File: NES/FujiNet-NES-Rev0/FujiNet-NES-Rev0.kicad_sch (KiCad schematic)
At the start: 0 parts

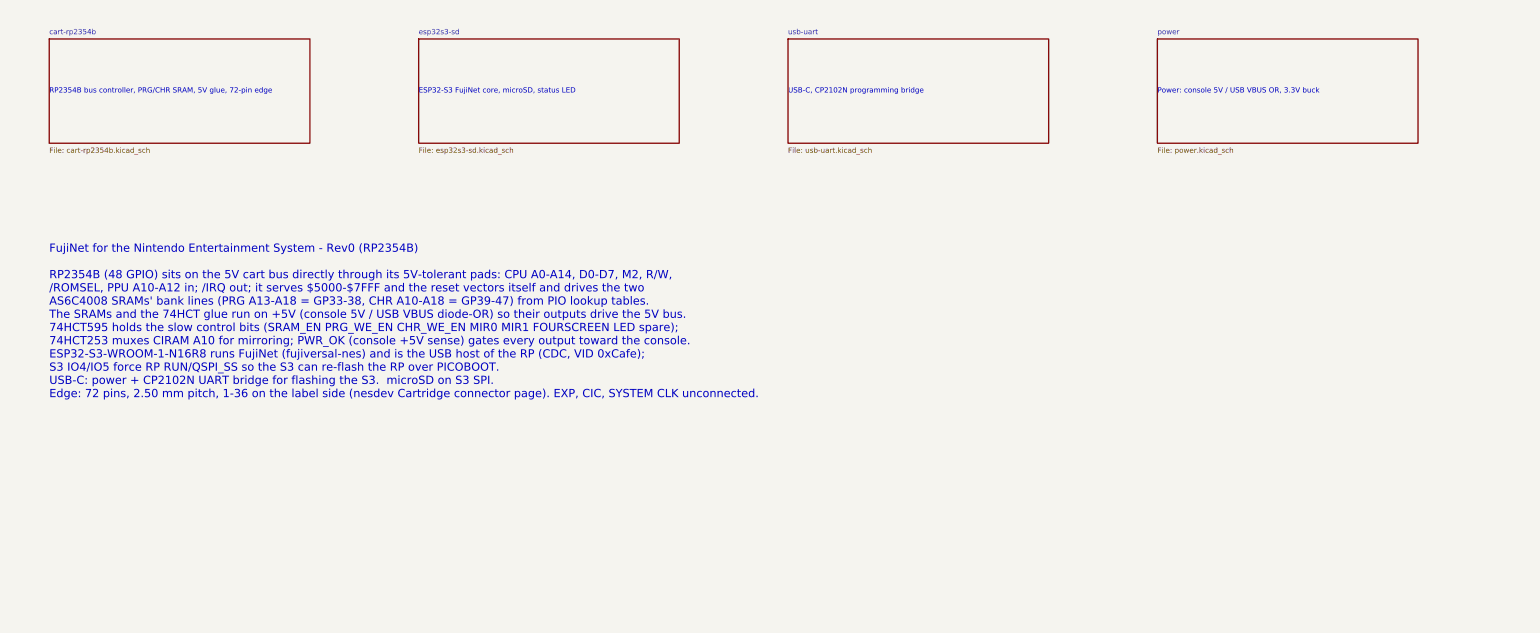
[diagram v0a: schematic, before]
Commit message: Nes rev0 (#48)
* NES: add the FujiNet-NES-Rev0 schematic

RP2354B on the 5 V cart bus with two AS6C4008-55 SRAMs (PRG, CHR) whose
bank lines come from the RP's PIO, 74HCT595/253/14/00/32 glue, and the
Astrocade Rev0 ESP32-S3, USB-UART and power sheets carried over.
Generated from tools/design.py the same way as Astrocade/rev0; ERC
reports no violations and tools/check_nets.py checks every GPIO, SRAM
line and decode equation against fujinet-firmware's nes_cart.h and
fujiversal-nes.h.

Schematic only: no layout, no board built, nothing run on a console.
The edge pinout follows the nesdev Cartridge connector page (pin 37 is
SYSTEM CLK, 2.50 mm pitch).

Co-Authored-By: Claude Fable 5.1 <noreply@anthropic.com>

* NES Rev0: audit the schematic with kicad-happy and redo it

Datasheet-backed review of the first Rev0 schematic (kicad-happy analyzer,
ngspice, 28 deep-review findings all evidence-gated, 453 netlist checks
against fujinet-firmware nes-bringup) and the fixes it called for:

- edge footprint was mirrored (pin 1 west); nesdev and two measured
  NES-EWROM-01 references put pin 1 east on the label side. Fingers are now
  2.0 x 12 mm (ends 3.0 at +/-44.25), 2.50 pitch, copper 1.0-13.0 mm in,
  Nintendo's front/back mask depths
- RP2350 pads are 5 V-tolerant only while IOVDD is powered: the IOVDD group
  moves to an AP2112K (20 us) rail +3V3_RP; VREG_VIN stays on the buck
- 74HCT595 /OE = NAND(PWR_OK, POR) with 100k pull-downs on every bit, so
  the register cannot enable the SRAMs before the RP loads it or while
  the console is off
- PRG /WE = NAND4(M2, ROMSEL, !R/W, PRG_WE_EN) on a CD74HCT20, one gate
  after M2 (was three after the console's /ROMSEL decoder vs ~30 ns hold)
- CIRAM /CE through the 74HCT253's second half, tri-stated by PWR_OK_N
- console 5 V through an AO3401A P-FET (gate = VBUS) instead of a Schottky
- console-sense divider 22k/100k (TI 74HCT14 VT+ reaches 0.70 x VCC)
- WS2812B-2020 on +5V (datasheet VDD 3.7-5.3 V, VIH 2.7 V)
- VBUS decoupling at t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
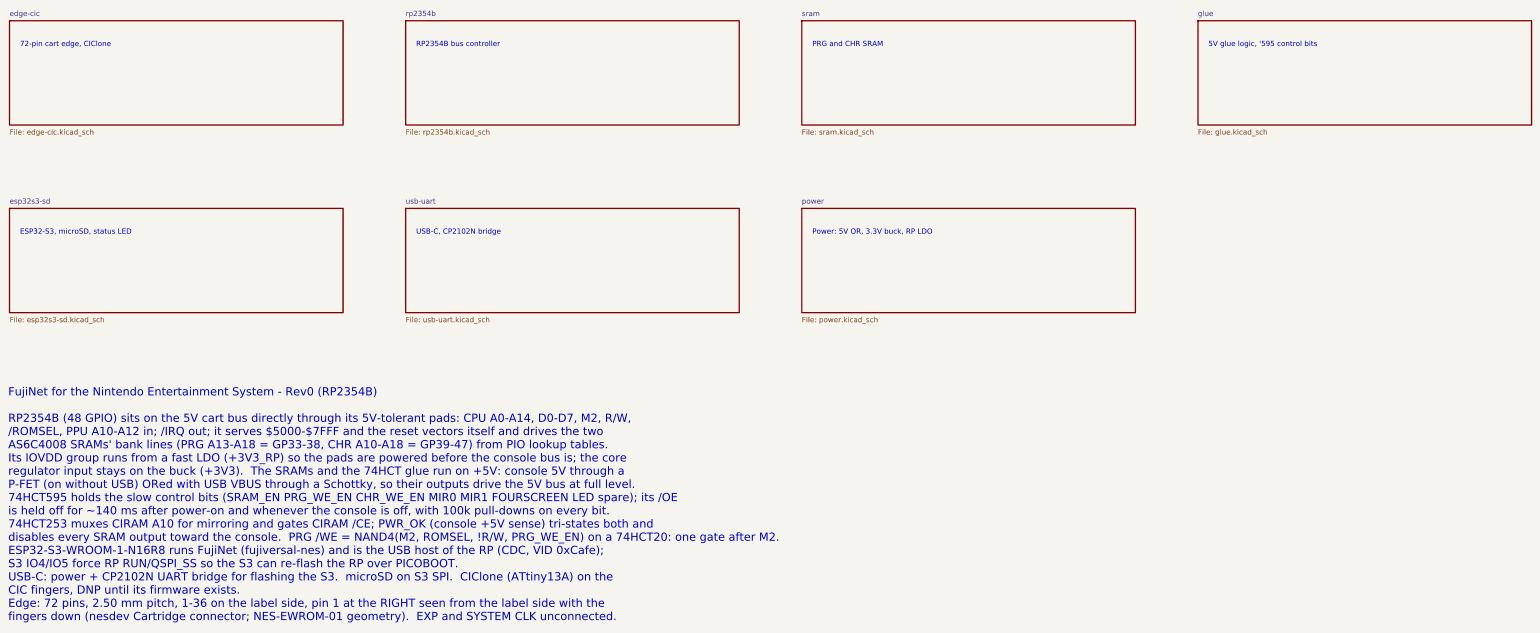
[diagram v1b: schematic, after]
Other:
- removed sheet cart-rp2354b
- added sheet edge-cic (edge-cic.kicad_sch)
- added sheet glue (glue.kicad_sch)
- added sheet rp2354b (rp2354b.kicad_sch)
- added sheet sram (sram.kicad_sch)
- note added: "5V glue logic, '595 control bits"
- note added: "72-pin cart edge, CIClone"
- note added: "ESP32-S3, microSD, status LED"
- note added: "FujiNet for the Nintendo Entertainment System - Rev0 (RP2354B) RP2354B (48 GPIO) sits on the 5V cart bus directly through its 5V-tolerant pads: CPU A0-A14, D0-D7, M2, R/W, /ROMSEL, PPU A10-A12 in; /IRQ out; it serves $5000-$7FFF and the reset vectors itself and drives the two AS6C4008 SRAMs' bank lines (PRG A13-A18 = GP33-38, CHR A10-A18 = GP39-47) from PIO lookup tables. Its IOVDD group runs fro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"
- note added: "PRG and CHR SRAM"
- note added: "Power: 5V OR, 3.3V buck, RP LDO"
- note added: "RP2354B bus controller"
- note added: "USB-C, CP2102N bridge"
- note removed: "ESP32-S3 FujiNet core, microSD, status LED"
- note removed: "FujiNet for the Nintendo Entertainment System - Rev0 (RP2354B) RP2354B (48 GPIO) sits on the 5V cart bus directly through its 5V-tolerant pads: CPU A0-A14, D0-D7, M2, R/W, /ROMSEL, PPU A10-A12 in; /IRQ out; it serves $5000-$7FFF and the reset vectors itself and drives the two AS6C4008 SRAMs' bank lines (PRG A13-A18 = GP33-38, CHR A10-A18 = GP39-47) from PIO lookup tables. The SRAMs and the 74HCT 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"
- note removed: "Power: console 5V / USB VBUS OR, 3.3V buck"
- note removed: "RP2354B bus controller, PRG/CHR SRAM, 5V glue, 72-pin edge"
- note removed: "USB-C, CP2102N programming bridge"
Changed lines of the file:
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@@
 	(title_block
 		(title "FujiNet NES Rev0")
-		(date "2026-09-30")
+		(date "2026-10-04")
 		(rev "0")
 		(company "FujiNet")
@@
 	)
 	(sheet
-		(at 30 40)
-		(size 63.5 25.4)
-		(fields_autoplaced yes)
-		(stroke
-			(width 0.12)
-			(type solid)
-		)
-		(fill
-			(color 0 0 0 0)
-		)
-		(property "Sheetname" "cart-rp2354b"
-			(at 30 39 0)
-			(effects
-				(font
-					(size 1.27 1.27)
-				)
-				(justify left bottom)
-			)
-		)
-		(property "Sheetfile" "cart-rp2354b.kicad_sch"
-			(at 30 66.4 0)
+		(at 20.32 35.56)
+		(size 81.28 25.4)
+		(fields_autoplaced yes)
+		(stroke
+			(width 0.12)
+			(type solid)
+		)
+		(fill
+			(color 0 0 0 0)
+		)
+		(property "Sheetname" "edge-cic"
+			(at 20.32 34.56 0)
+			(effects
+				(font
+					(size 1.27 1.27)
+				)
+				(justify left bottom)
+			)
+		)
+		(property "Sheetfile" "edge-cic.kicad_sch"
+			(at 20.32 61.96 0)
 			(effects
 				(font
@@
 		)
 	)
-	(text "RP2354B bus controller, PRG/CHR SRAM, 5V glue, 72-pin edge"
-		(exclude_from_sim no)
-		(at 30 52.7 0)
-		(effects
-			(font
-				(size 1.27 1.27)
-			)
-			(justify left)
-		)
-	)
-	(sheet
-		(at 120 40)
-		(size 63.5 25.4)
+	(text "72-pin cart edge, CIClone"
+		(exclude_from_sim no)
+		(at 22.86 40.64 0)
+		(effects
+			(font
+				(size 1.27 1.27)
+			)
+			(justify left top)
+		)
+	)
+	(sheet
+		(at 116.84 35.56)
+		(size 81.28 25.4)
+		(fields_autoplaced yes)
+		(stroke
+			(width 0.12)
+			(type solid)
+		)
+		(fill
+			(color 0 0 0 0)
+		)
+		(property "Sheetname" "rp2354b"
+			(at 116.84 34.56 0)
+			(effects
+				(font
+					(size 1.27 1.27)
+				)
+				(justify left bottom)
+			)
+		)
+		(property "Sheetfile" "rp2354b.kicad_sch"
+			(at 116.84 61.96 0)
+			(effects
+				(font
+					(size 1.27 1.27)
+				)
+				(justify left top)
+			)
+		)
+		(instances
+			(project "FujiNet-NES-Rev0"
+				(path "/5810f54f-2240-53c0-bbad-5b0b7a2c3f6b"
+					(page "3")
+				)
+			)
+		)
+	)
+	(text "RP2354B bus controller"
+		(exclude_from_sim no)
+		(at 119.38 40.64 0)
+		(effects
+			(font
+				(size 1.27 1.27)
+			)
+			(justify left top)
+		)
+	)
+	(sheet
+		(at 213.36 35.56)
+		(size 81.28 25.4)
+		(fields_autoplaced yes)
+		(stroke
+			(width 0.12)
+			(type solid)
+		)
+		(fill
+			(color 0 0 0 0)
+		)
+		(property "Sheetname" "sram"
+			(at 213.36 34.56 0)
+			(effects
+				(font
+					(size 1.27 1.27)
+				)
+				(justify left bottom)
+			)
+		)
+		(property "Sheetfile" "sram.kicad_sch"
+			(at 213.36 61.96 0)
+			(effects
+				(font
+					(size 1.27 1.27)
+				)
+				(justify left top)
+			)
+		)
+		(instances
+			(project "FujiNet-NES-Rev0"
+				(path "/5810f54f-2240-53c0-bbad-5b0b7a2c3f6b"
+					(page "4")
+				)
+			)
+		)
+	)
+	(text "PRG and CHR SRAM"
+		(exclude_from_sim no)
+		(at 215.9 40.64 0)
+		(effects
+			(font
+				(size 1.27 1.27)
+			)
+			(justify left top)
+		)
+	)
+	(sheet
+		(at 309.88 35.56)
+		(size 81.28 25.4)
+		(fields_autoplaced yes)
+		(stroke
+			(width 0.12)
+			(type solid)
+		)
+		(fill
+			(color 0 0 0 0)
+		)
+		(property "Sheetname" "glue"
+			(at 309.88 34.56 0)
+			(effects
+				(font
+					(size 1.27 1.27)
+				)
+				(justify left bottom)
+			)
+		)
+		(property "Sheetfile" "glue.kicad_sch"
+			(at 309.88 61.96 0)
+			(effects
+				(font
+					(size 1.27 1.27)
+				)
+				(justify left top)
+			)
+		)
+		(instances
+			(project "FujiNet-NES-Rev0"
+				(path "/5810f54f-2240-53c0-bbad-5b0b7a2c3f6b"
+					(page "5")
+				)
+			)
+		)
+	)
+	(text "5V glue logic, '595 control bits"
+		(exclude_from_sim no)
+		(at 312.42 40.64 0)
+		(effects
+			(font
+				(size 1.27 1.27)
+			)
+			(justify left top)
+		)
+	)
+	(sheet
+		(at 20.32 81.28)
+		(size 81.28 25.4)
 		(fields_autoplaced yes)
 		(stroke
@@
 		)
 		(property "Sheetname" "esp32s3-sd"
-			(at 120 39 0)
+			(at 20.32 80.28 0)
 			(effects
 				(font
@@
 		)
 		(property "Sheetfile" "esp32s3-sd.kicad_sch"
-			(at 120 66.4 0)
-			(effects
-				(font
-					(size 1.27 1.27)
-				)
-				(justify left top)
-			)
-		)
-		(instances
-			(project "FujiNet-NES-Rev0"
-				(path "/5810f54f-2240-53c0-bbad-5b0b7a2c3f6b"
-					(page "3")
-				)
-			)
-		)
-	)
-	(text "ESP32-S3 FujiNet core, microSD, status LED"
-		(exclude_from_sim no)
-		(at 120 52.7 0)
-		(effects
-			(font
-				(size 1.27 1.27)
-			)
-			(justify left)
-		)
-	)
-	(sheet
-		(at 210 40)
-		(size 63.5 25.4)
+			(at 20.32 107.68 0)
+			(effects
+				(font
+					(size 1.27 1.27)
+				)
+				(justify left top)
+			)
+		)
+		(instances
+			(project "FujiNet-NES-Rev0"
+				(path "/5810f54f-2240-53c0-bbad-5b0b7a2c3f6b"
+					(page "6")
+				)
+			)
+		)
+	)
+	(text "ESP32-S3, microSD, status LED"
+		(exclude_from_sim no)
+		(at 22.86 86.36 0)
+		(effects
+			(font
+				(size 1.27 1.27)
+			)
+			(justify left top)
+		)
+	)
+	(sheet
+		(at 116.84 81.28)
+		(size 81.28 25.4)
 		(fields_autoplaced yes)
 		(stroke
@@
 		)
 		(property "Sheetname" "usb-uart"
-			(at 210 39 0)
+			(at 116.84 80.28 0)
 			(effects
 				(font
@@
 		)
 		(property "Sheetfile" "usb-uart.kicad_sch"
-			(at 210 66.4 0)
-			(effects
-				(font
-					(size 1.27 1.27)
-				)
-				(justify left top)
-			)
-		)
-		(instances
-			(project "FujiNet-NES-Rev0"
-				(path "/5810f54f-2240-53c0-bbad-5b0b7a2c3f6b"
-					(page "4")
-				)
-			)
-		)
-	)
-	(text "USB-C, CP2102N programming bridge"
-		(exclude_from_sim no)
-		(at 210 52.7 0)
-		(effects
-			(font
-				(size 1.27 1.27)
-			)
-			(justify left)
-		)
-	)
-	(sheet
-		(at 300 40)
-		(size 63.5 25.4)
+			(at 116.84 107.68 0)
+			(effects
+				(font
+					(size 1.27 1.27)
+				)
+				(justify left top)
+			)
+		)
+		(instances
+			(project "FujiNet-NES-Rev0"
+				(path "/5810f54f-2240-53c0-bbad-5b0b7a2c3f6b"
+					(page "7")
+				)
+			)
+		)
+	)
+	(text "USB-C, CP2102N bridge"
+		(exclude_from_sim no)
+		(at 119.38 86.36 0)
+		(effects
+			(font
+				(size 1.27 1.27)
+			)
+			(justify left top)
+		)
+	)
+	(sheet
+		(at 213.36 81.28)
+		(size 81.28 25.4)
 		(fields_autoplaced yes)
 		(stroke
@@
 		)
 		(property "Sheetname" "power"
-			(at 300 39 0)
+			(at 213.36 80.28 0)
 			(effects
 				(font
@@
 		)
 		(property "Sheetfile" "power.kicad_sch"
-			(at 300 66.4 0)
-			(effects
-				(font
-					(size 1.27 1.27)
-				)
-				(justify left top)
-			)
-		)
-		(instances
-			(project "FujiNet-NES-Rev0"
-				(path "/5810f54f-2240-53c0-bbad-5b0b7a2c3f6b"
-					(page "5")
-				)
-			)
-		)
-	)
-	(text "Power: console 5V / USB VBUS OR, 3.3V buck"
-		(exclude_from_sim no)
-		(at 300 52.7 0)
-		(effects
-			(font
-				(size 1.27 1.27)
-			)
-			(justify left)
-		)
-	)
-	(text "FujiNet for the Nintendo Entertainment System - Rev0 (RP2354B)\n\nRP2354B (48 GPIO) sits on the 5V cart bus directly through its 5V-tolerant pads: CPU A0-A14, D0-D7, M2, R/W,\n/ROMSEL, PPU A10-A12 in; /IRQ out; it serves $5000-$7FFF and the reset vectors itself and drives the two\nAS6C4008 SRAMs' bank lines (PRG A13-A18 = GP33-38, CHR A10-A18 = GP39-47) from PIO lookup tables.\nThe SRAMs and the 74HCT glue run on +5V (console 5V / USB VBUS diode-OR) so their outputs drive the 5V bus.\n74HCT595 holds the slow control bits (SRAM_EN PRG_WE_EN CHR_WE_EN MIR0 MIR1 FOURSCREEN LED spare);\n74HCT253 muxes CIRAM A10 for mirroring; PWR_OK (console +5V sense) gates every output toward the console.\nESP32-S3-WROOM-1-N16R8 runs FujiNet (fujiversal-nes) and is the USB host of the RP (CDC, VID 0xCafe);\nS3 IO4/IO5 force RP RUN/QSPI_SS so the S3 can re-flash the RP over PICOBOOT.\nUSB-C: power + CP2102N UART bridge for flashing the S3.  microSD on S3 SPI.\nEdge: 72 pins, 2.50 mm pitch, 1-36 on the label side (nesdev Cartridge connector page). EXP, CIC, SYSTEM CLK unconnected."
-		(exclude_from_sim no)
-		(at 30 90 0)
-		(effects
-			(font
+			(at 213.36 107.68 0)
+			(effects
+				(font
+					(size 1.27 1.27)
+				)
+				(justify left top)
+			)
+		)
+		(instances
+			(project "FujiNet-NES-Rev0"
+				(path "/5810f54f-2240-53c0-bbad-5b0b7a2c3f6b"
+					(page "8")
+				)
+			)
+		)
+	)
+	(text "Power: 5V OR, 3.3V buck, RP LDO"
+		(exclude_from_sim no)
+		(at 215.9 86.36 0)
+		(effects
+			(font
+				(size 1.27 1.27)
+			)
+			(justify left top)
+		)
+	)
+	(text "FujiNet for the Nintendo Entertainment System - Rev0 (RP2354B)\n\nRP2354B (48 GPIO) sits on the 5V cart bus directly through its 5V-tolerant pads: CPU A0-A14, D0-D7, M2, R/W,\n/ROMSEL, PPU A10-A12 in; /IRQ out; it serves $5000-$7FFF and the reset vectors itself and drives the two\nAS6C4008 SRAMs' bank lines (PRG A13-A18 = GP33-38, CHR A10-A18 = GP39-47) from PIO lookup tables.\nIts IOVDD group runs from a fast LDO (+3V3_RP) so the pads are powered before the console bus is; the core\nregulator input stays on the buck (+3V3).  The SRAMs and the 74HCT glue run on +5V: console 5V through a\nP-FET (on without USB) ORed with USB VBUS through a Schottky, so their outputs drive the 5V bus at full level.\n74HCT595 holds the slow control bits (SRAM_EN PRG_WE_EN CHR_WE_EN MIR0 MIR1 FOURSCREEN LED spare); its /OE\nis held off for ~140 ms after power-on and whenever the console is off, with 100k pull-downs on every bit.\n74HCT253 muxes CIRAM A10 for mirroring and gates CIRAM /CE; PWR_OK (console +5V sense) tri-states both and\ndisables every SRAM output toward the console.  PRG /WE = NAND4(M2, ROMSEL, !R/W, PRG_WE_EN) on a 74HCT20: one gate after M2.\nESP32-S3-WROOM-1-N16R8 runs FujiNet (fujiversal-nes) and is the USB host of the RP (CDC, VID 0xCafe);\nS3 IO4/IO5 force RP RUN/QSPI_SS so the S3 can re-flash the RP over PICOBOOT.\nUSB-C: power + CP2102N UART bridge for flashing the S3.  microSD on S3 SPI.  CIClone (ATtiny13A) on the\nCIC fingers, DNP until its firmware exists.\nEdge: 72 pins, 2.50 mm pitch, 1-36 on the label side, pin 1 at the RIGHT seen from the label side with the\nfingers down (nesdev Cartridge connector; NES-EWROM-01 geometry).  EXP and SYSTEM CLK unconnected."
+		(exclude_from_sim no)
+		(at 20 125 0)
+		(effects
+			(font
